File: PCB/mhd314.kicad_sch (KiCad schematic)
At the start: 3 parts, among them J1 Raspberry_Pi_2_3, J2 AudioJack3, J3 AudioJack4

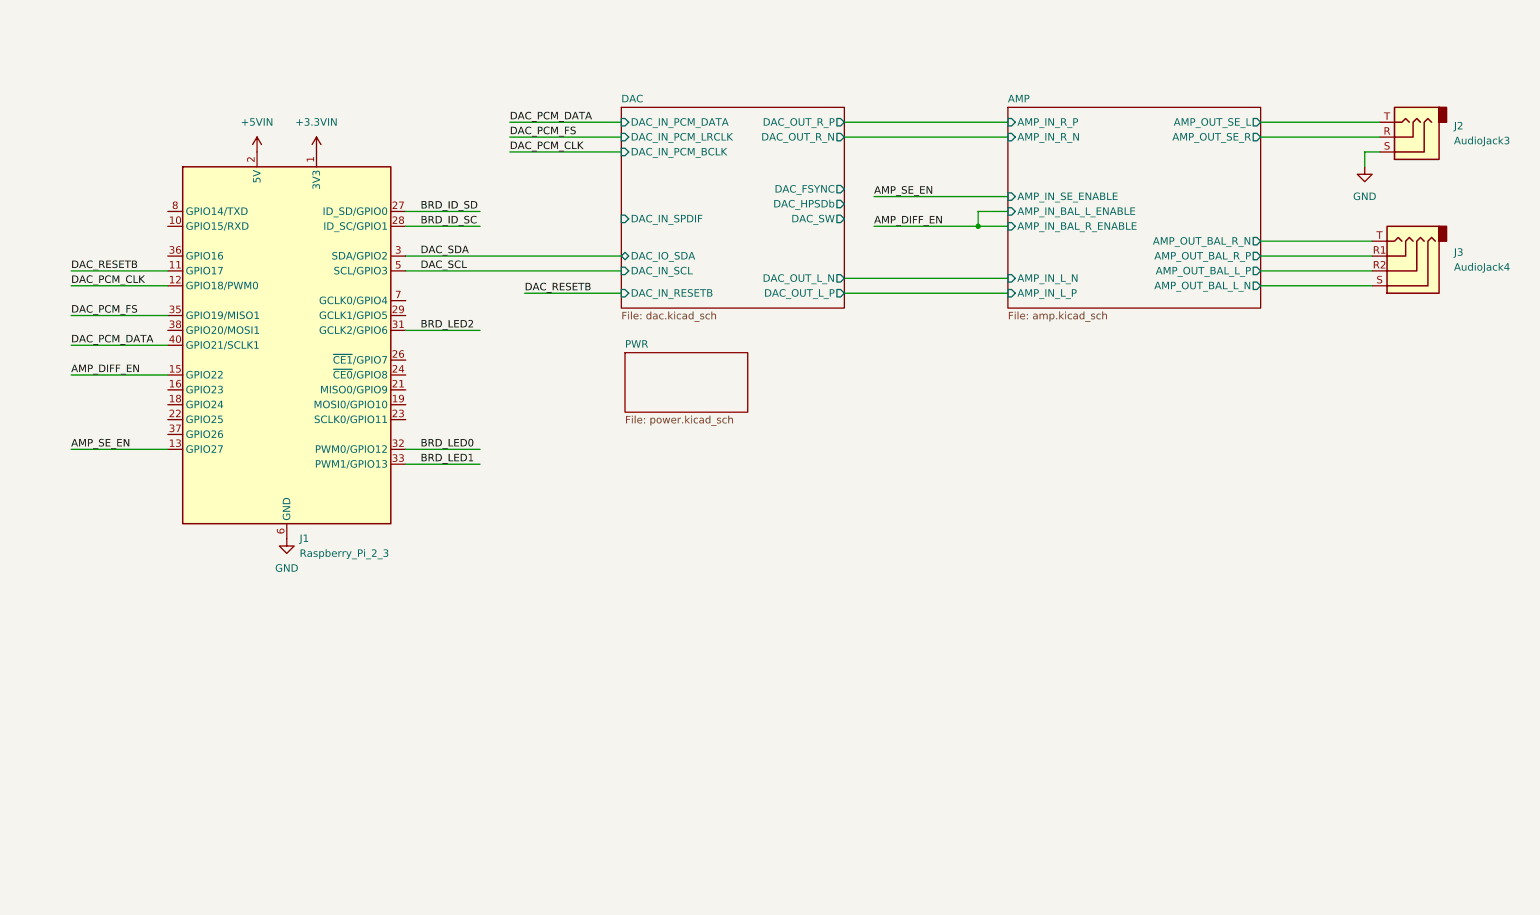
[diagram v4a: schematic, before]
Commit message: Added E2P and testpoints
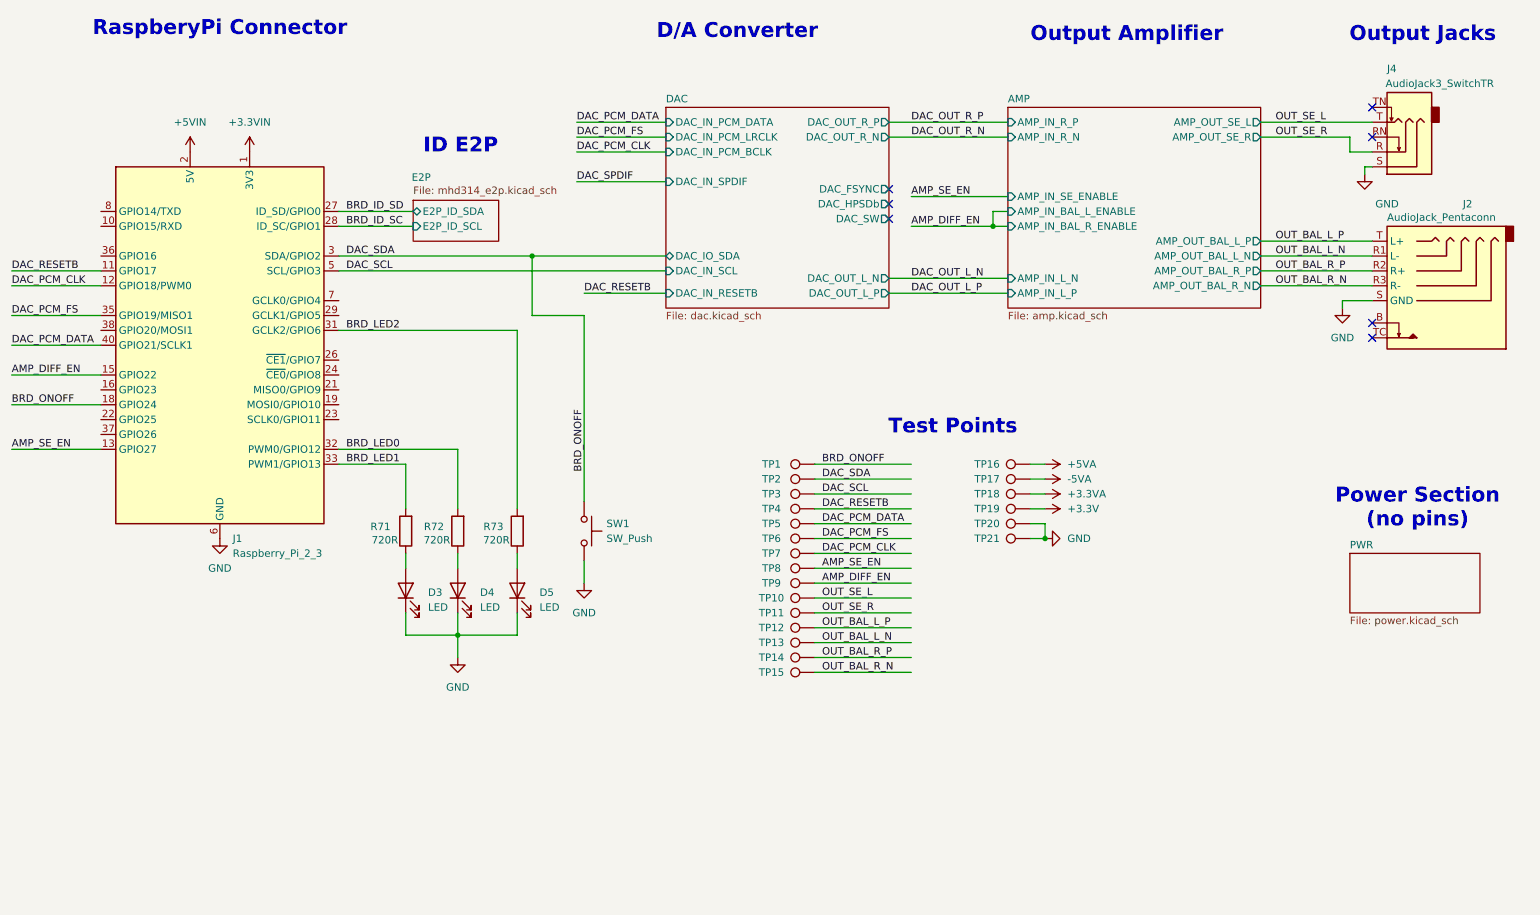
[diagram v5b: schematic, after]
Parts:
- removed J2: AudioJack3, symbol Connector_Audio:AudioJack3
- removed J3: AudioJack4, symbol Connector_Audio:AudioJack4
- added D3, D4, D5: LED, LED_SMD:LED_0603_1608Metric_Pad1.05x0.95mm_HandSolder, symbol Device:LED
- added J2: AudioJack_Pentaconn, _mahaudio KiCad Library:Jack_4.4mm_Pentaconn_NBA1-24-001_Horizontal, symbol mahaudio_kicad_lib:AudioJack_Pentaconn
- added J4: AudioJack3_SwitchTR, _mahaudio KiCad Library:Jack_3.5mm_CUI_SJ1-3535NG_Horizontal_3D, symbol Connector_Audio:AudioJack3_SwitchTR
- added R71, R72, R73: 720R, Resistor_SMD:R_0402_1005Metric_Pad0.72x0.64mm_HandSolder, symbol Device:R
- added SW1: SW_Push, Button_Switch_THT:SW_Tactile_SPST_Angled_PTS645Vx39-2LFS, symbol Switch:SW_Push
- added TP1, TP10, TP11, TP12, TP13, TP14, TP15, TP16, TP17, TP18, TP19, TP2, TP20, TP21, TP3, TP4, TP5, TP6, TP7, TP8, TP9: TestPoint, TestPoint:TestPoint_Pad_D1.0mm, symbol Connector:TestPoint
- J1: footprint (none) -> Connector_PinHeader_2.54mm:PinHeader_2x20_P2.54mm_Vertical
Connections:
- net DAC_SDA is gone; now on net BRD_ONOFF: J1.3 (SDA/GPIO2)
- net AMP_DIFF_EN: now also TP9.1
- net AMP_SE_EN: now also TP8.1
- net BRD_LED0: now also R72.2
- net BRD_LED1: now also R71.2
- net BRD_LED2: now also R73.2
- net DAC_PCM_CLK: now also TP7.1
- net DAC_PCM_DATA: now also TP5.1
- net DAC_PCM_FS: now also TP6.1
- net DAC_RESETB: now also TP4.1
- net DAC_SCL: now also TP3.1
- net GND: now also D3.1 (K), D4.1 (K), D5.1 (K), J2.S (GND), J4.S, SW1.2, TP20.1, TP21.1
- net BRD_ONOFF: now reaches J1.18 (GPIO24)
- net BRD_ONOFF: now also SW1.1, TP1.1, TP2.1
- new net: D4.2 (A), R72.1
- new net: D3.2 (A), R71.1
- new net: D5.2 (A), R73.1
- new net +3.3V: TP19.1
- new net +3.3VA: TP18.1
- new net +5VA: TP16.1
- new net -5VA: TP17.1
- new net OUT_BAL_L_N: J2.R1 (L-), TP13.1
- new net OUT_BAL_L_P: J2.T (L+), TP12.1
- new net OUT_BAL_R_N: J2.R3 (R-), TP15.1
- new net OUT_BAL_R_P: J2.R2 (R+), TP14.1
- new net OUT_SE_L: J4.T, TP10.1
- new net OUT_SE_R: J4.R, TP11.1
- no-connect marks 0 -> 7
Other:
- added sheet E2P (mhd314_e2p.kicad_sch)
- note added: "D/A Converter"
- note added: "ID E2P"
- note added: "Output Amplifier"
- note added: "Output Jacks"
- note added: "Power Section (no pins)"
- note added: "RaspberyPi Connector"
- note added: "Test Points"
- moved on the sheet: J1

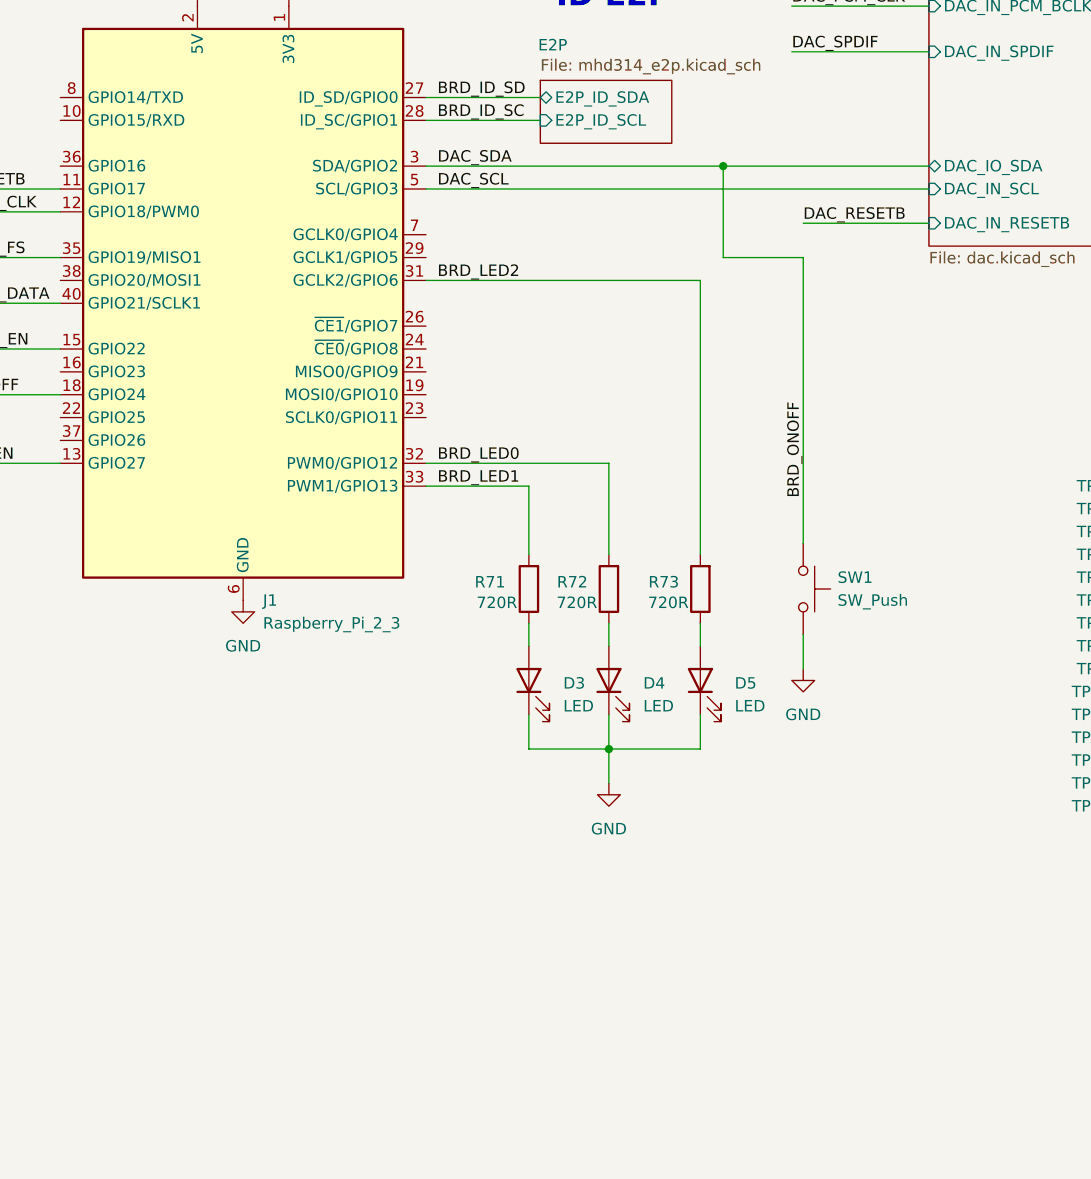
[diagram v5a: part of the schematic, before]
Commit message: PCB drawn with connector placement ok
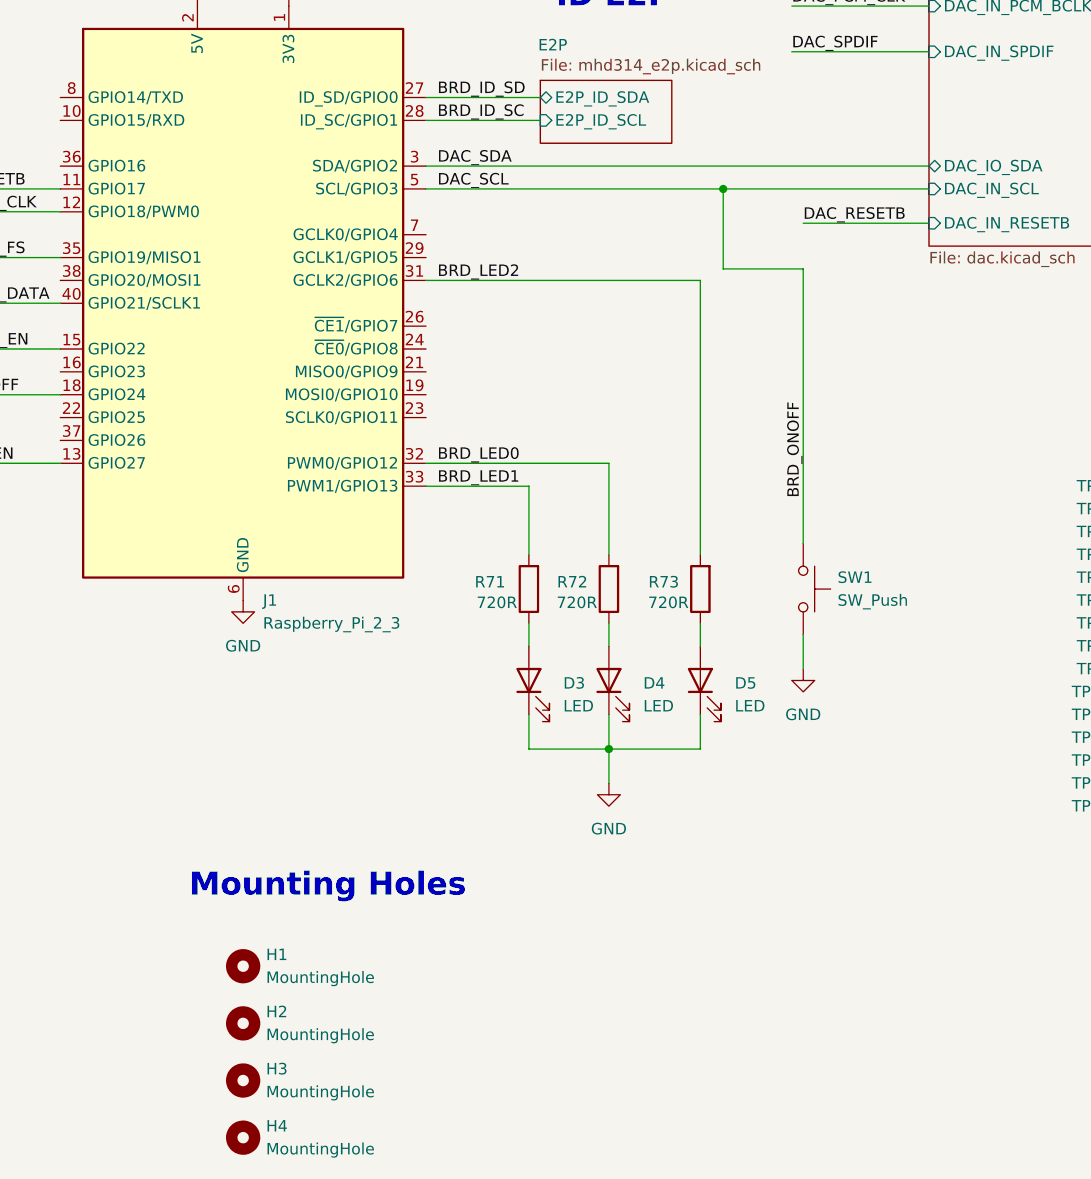
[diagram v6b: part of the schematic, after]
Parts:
- added H1, H2, H3, H4: MountingHole, MountingHole:MountingHole_2.7mm_M2.5_DIN965_Pad, symbol Mechanical:MountingHole
- J1: footprint Connector_PinHeader_2.54mm:PinHeader_2x20_P2.54mm_Vertical -> Connector_PinSocket_2.54mm:PinSocket_2x20_P2.54mm_Vertical
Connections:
- net DAC_SCL is gone; now on net BRD_ONOFF: J1.5 (SCL/GPIO3), TP3.1
- net BRD_ONOFF: no longer J1.3 (SDA/GPIO2), TP2.1
- new net DAC_SDA: J1.3 (SDA/GPIO2), TP2.1
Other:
- note added: "Mounting Holes"

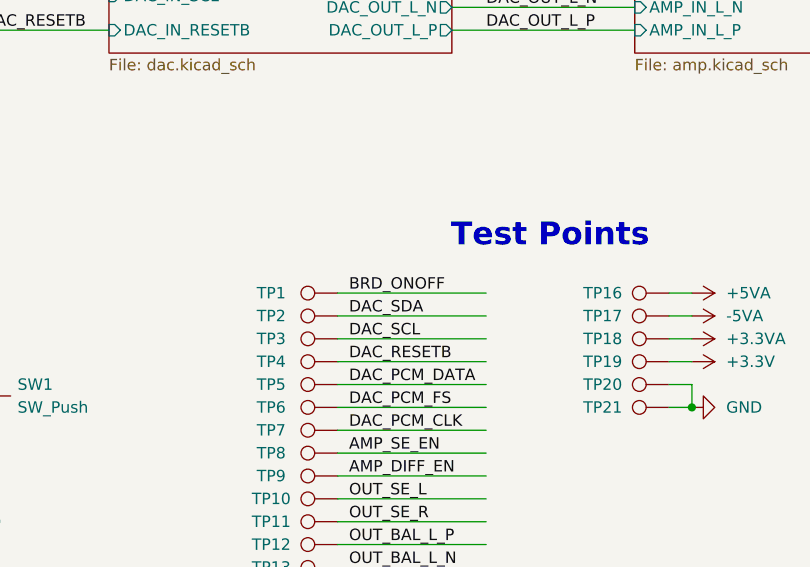
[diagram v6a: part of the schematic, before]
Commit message: Finished basic placement
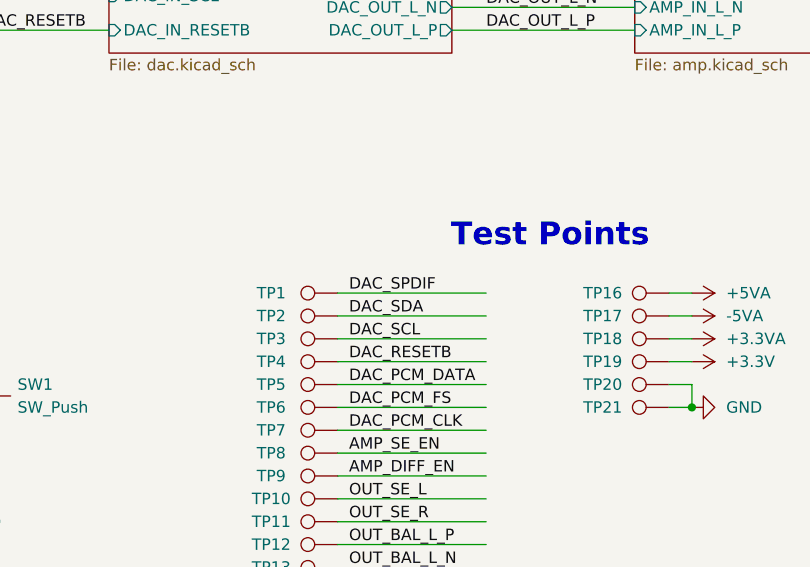
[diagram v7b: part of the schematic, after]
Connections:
- net BRD_ONOFF: no longer TP1.1
- net DAC_SPDIF: now also TP1.1
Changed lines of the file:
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@@
+		)
+	)
+	(label "DAC_SPDIF"
+		(at 160.02 105.41 0)
+		(fields_autoplaced yes)
+		(effects
+			(font
+				(size 1.27 1.27)
+			)
+			(justify left bottom)
 		)
 	)
@@
 		(fields_autoplaced yes)
 		(effects
-			(font
-				(size 1.27 1.27)
-			)
-			(justify left bottom)
-		)
-	)
-	(label "BRD_ONOFF"
-		(at 160.02 105.41 0)
-		(fields_autoplaced yes)
-		(effects
